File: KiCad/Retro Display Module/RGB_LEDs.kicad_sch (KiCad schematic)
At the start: 25 parts, among them J21 Conn_01x02_Pin, J23 Conn_01x02_Pin, J24 Conn_01x04_Pin, J25 Conn_02x03_Odd_Even, U4 2N7002

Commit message: Updated USB PD and Driver LED circuit
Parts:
- TP1, TP2, TP3: footprint TestPoint:TestPoint_Pad_2.0x2.0mm -> Library:TestPoint_THTPad_2.0x2.0mm_Drill1.0mm
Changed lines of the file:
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@@
       (effects (font (size 1.27 1.27)) (justify left))
     )
-    (property "Footprint" "TestPoint:TestPoint_Pad_2.0x2.0mm" (at 156.21 163.83 0)
+    (property "Footprint" "Library:TestPoint_THTPad_2.0x2.0mm_Drill1.0mm" (at 156.21 163.83 0)
       (effects (font (size 1.27 1.27)) hide)
     )
@@
         )
         (path "/046eef48-6d3f-4288-a12a-fc20b7e12e30/5f242e7d-44cc-4d59-bac4-986620e81512"
-          (reference "#PWR016") (unit 1)
+          (reference "#PWR017") (unit 1)
         )
       )
@@
         )
         (path "/046eef48-6d3f-4288-a12a-fc20b7e12e30/5f242e7d-44cc-4d59-bac4-986620e81512"
-          (reference "#PWR017") (unit 1)
+          (reference "#PWR018") (unit 1)
         )
       )
@@
       (effects (font (size 1.27 1.27)) (justify left))
     )
-    (property "Footprint" "TestPoint:TestPoint_Pad_2.0x2.0mm" (at 87.63 162.56 0)
+    (property "Footprint" "Library:TestPoint_THTPad_2.0x2.0mm_Drill1.0mm" (at 87.63 162.56 0)
       (effects (font (size 1.27 1.27)) hide)
     )
@@
       (effects (font (size 1.27 1.27)) (justify left))
     )
-    (property "Footprint" "TestPoint:TestPoint_Pad_2.0x2.0mm" (at 123.19 162.56 0)
-      (effects (font (size 1.27 1.27)) hide)
-    )
+    (property "Footprint" "Library:TestPoint_THTPad_2.0x2.0mm_Drill1.0mm" (at 123.19 162.56 0)
+      (effects (font (size 1.27 1.27)) hide)
+    )

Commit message: Begin STM32 Programming
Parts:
- removed D1, D11, D13, D15, D17, D19, D21, D3, D5, D7, D9: WS2812B, Library:LED-SMD_4P-L5.0-W5.0-BL_XL-5050RGBC, symbol LED:WS2812B
- added D10, D11, D12, D13, D14, D15, D16, D17, D18, D19, D20, D21, D22, D23, D3, D4, D5, D6, D7, D8, D9: XL-1615RGBC-WS2812B, Library:LED-SMD_4P-L1.6-W1.5_XL-1615RGBC-WS2812B, symbol EEE4022S:XL-1615RGBC-WS2812B
- J21, J23, J24: now left out of the parts list
- TP1, TP2, TP3: now not fitted; now left out of the parts list
- renumbered J25 to J27
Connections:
- net Cheese: now also D5.4 (DI)
- net DIN: now also D3.4 (DI), D4.4 (DI)
- net GND: now also D10.3 (GND), D11.3 (GND), D12.3 (GND), D13.3 (GND), D14.3 (GND), D15.3 (GND), D16.3 (GND), D17.3 (GND), D18.3 (GND), D19.3 (GND), D20.3 (GND), D21.3 (GND), D22.3 (GND), D23.3 (GND), D3.3 (GND), D4.3 (GND), D5.3 (GND), D6.3 (GND), D7.3 (GND), D8.3 (GND), D9.3 (GND)
- net at J21.1 (Pin_1): now also D10.2 (VDD), D11.2 (VDD), D12.2 (VDD), D13.2 (VDD), D14.2 (VDD), D15.2 (VDD), D16.2 (VDD), D17.2 (VDD), D18.2 (VDD), D19.2 (VDD), D20.2 (VDD), D21.2 (VDD), D22.2 (VDD), D23.2 (VDD), D3.2 (VDD), D4.2 (VDD), D6.2 (VDD), D7.2 (VDD), D8.2 (VDD), D9.2 (VDD)
- net at J23.1 (Pin_1), TP3.1: now also D5.1 (DO)
- net at D22.1 (K): now also D5.2 (VDD)
- new net: D12.1 (DO), D14.4 (DI)
- new net: D10.1 (DO), D12.4 (DI)
- new net: D13.1 (DO), D15.4 (DI)
- new net: D11.1 (DO), D13.4 (DI)
- new net: D16.1 (DO), D18.4 (DI)
- new net: D14.1 (DO), D16.4 (DI)
- new net: D19.1 (DO), D21.4 (DI)
- new net: D17.1 (DO), D19.4 (DI)
- new net: D7.1 (DO), D9.4 (DI)
- new net: D4.1 (DO), D7.4 (DI)
- new net: D6.1 (DO), D8.4 (DI)
- new net: D3.1 (DO), D6.4 (DI)
- new net: D15.1 (DO), D17.4 (DI)
- new net: D10.4 (DI), D8.1 (DO)
- new net: D20.1 (DO), D22.4 (DI)
- new net: D18.1 (DO), D20.4 (DI)
- new net: D11.4 (DI), D9.1 (DO)
- new net: D21.1 (DO), D23.4 (DI)
- no-connect marks 1 -> 2
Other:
- moved on the sheet: D22, J21, J23, J24, J27, R5, U4

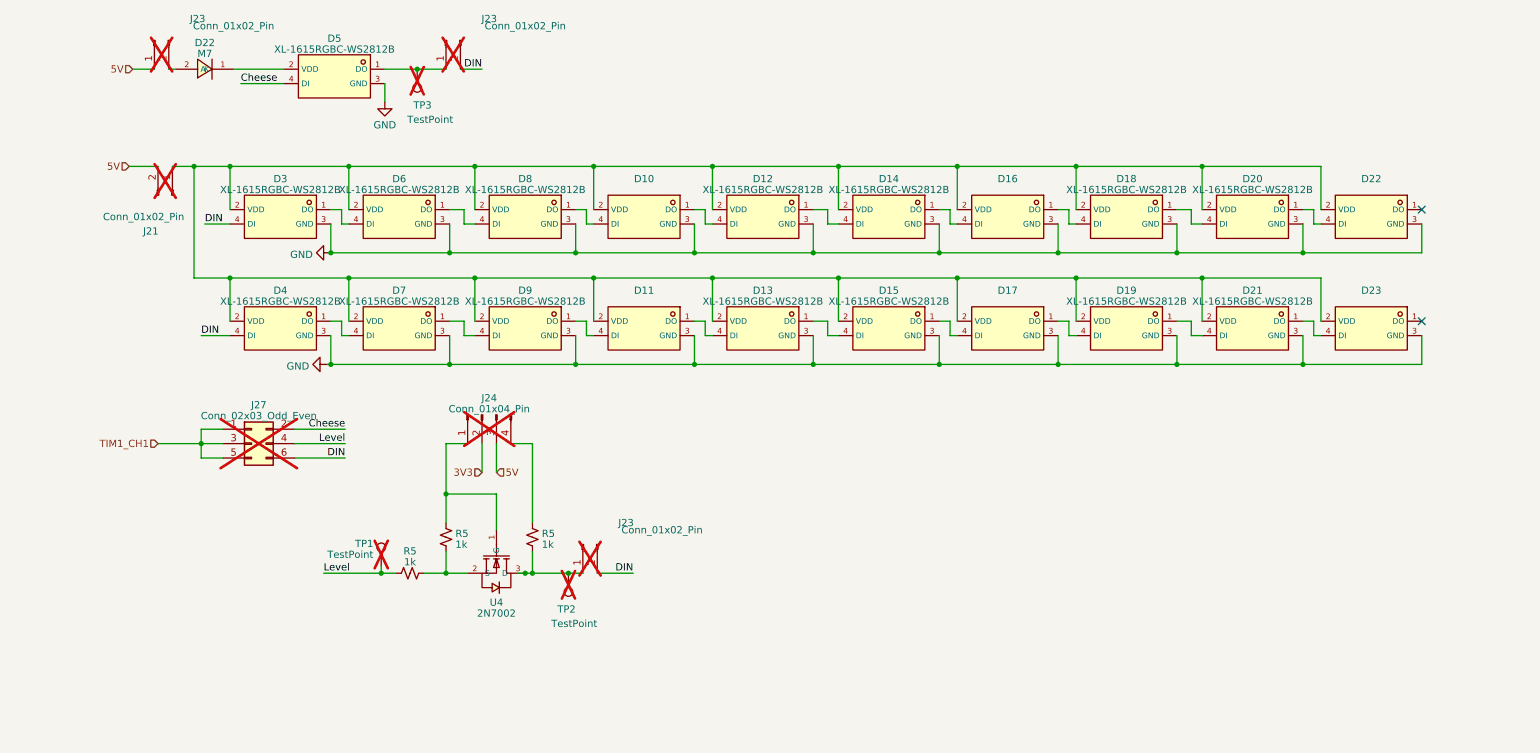
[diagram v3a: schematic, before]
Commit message: Updated Schematics and Added Reverse polarity protection
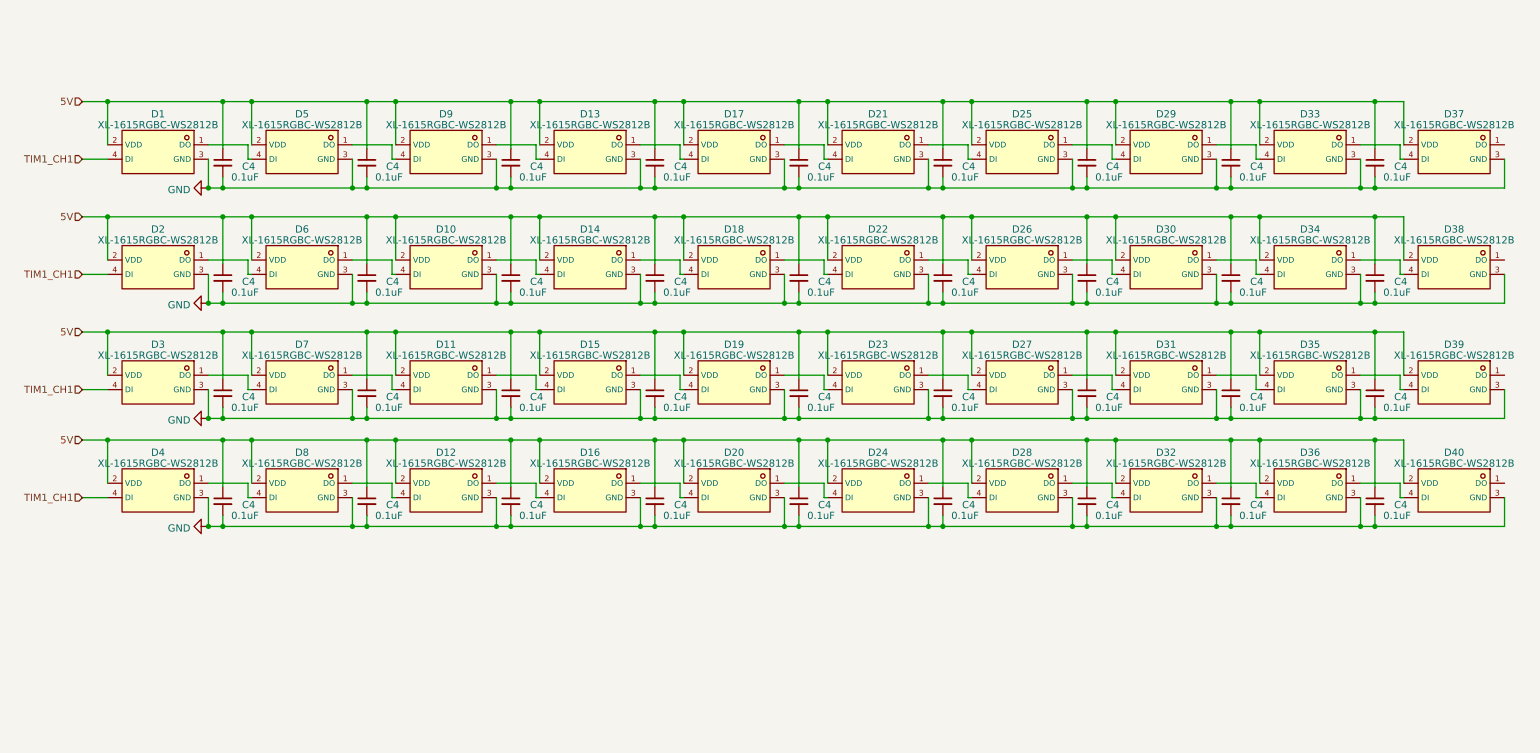
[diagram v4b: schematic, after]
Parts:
- removed D22: M7, Library:SMA_L4.3-W2.6-LS5.2-RD, symbol EEE4022S:M7_C95872
- removed J21, J23 (x3): Conn_01x02_Pin, Connector_PinHeader_2.54mm:PinHeader_1x02_P2.54mm_Vertical, symbol Connector:Conn_01x02_Pin
- removed J24: Conn_01x04_Pin, Connector_PinHeader_2.54mm:PinHeader_1x04_P2.54mm_Vertical, symbol Connector:Conn_01x04_Pin
- removed J27: Conn_02x03_Odd_Even, Connector_PinHeader_2.54mm:PinHeader_2x03_P2.54mm_Vertical, symbol Connector_Generic:Conn_02x03_Odd_Even
- removed R5 (x3): 1k, Resistor_SMD:R_0805_2012Metric, symbol Device:R_Small_US
- removed TP1, TP2, TP3: TestPoint, Library:TestPoint_THTPad_2.0x2.0mm_Drill1.0mm, symbol Connector:TestPoint
- removed U4: 2N7002, Library:SOT-23-3_L2.9-W1.3-P1.90-LS2.4-BR, symbol EEE4022S:AO3400A
- added C4 (x36): 0.1uF, Library:C_0402_1005Metric_Pad0.74x0.62mm_HandSolder, symbol Device:C_Small
- added D2, D24, D25, D26, D27, D28, D29, D3, D30, D31, D32, D33, D34, D35, D36, D37, D38, D39, D40: XL-1615RGBC-WS2812B, Library:LED-SMD_4P-L1.6-W1.5_XL-1615RGBC-WS2812B, symbol EEE4022S:XL-1615RGBC-WS2812B
- renumbered D3 to D1
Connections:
- net Cheese is gone; now on an unnamed net: D5.4 (DI)
- net DIN is gone; now on net TIM1_CH1: D1.4 (DI), D4.4 (DI)
- net 5V: now also D1.2 (VDD), D10.2 (VDD), D11.2 (VDD), D12.2 (VDD), D13.2 (VDD), D14.2 (VDD), D15.2 (VDD), D16.2 (VDD), D17.2 (VDD), D18.2 (VDD), D19.2 (VDD), D20.2 (VDD), D21.2 (VDD), D22.2 (VDD), D23.2 (VDD), D4.2 (VDD), D5.2 (VDD), D6.2 (VDD), D7.2 (VDD), D8.2 (VDD), D9.2 (VDD), C4.1, C4.1, C4.1, C4.1, C4.1, C4.1, C4.1, C4.1, C4.1, C4.1, C4.1, C4.1, C4.1, C4.1, C4.1, C4.1, C4.1, C4.1, C4.1, C4.1, C4.1, C4.1, C4.1, C4.1, C4.1, C4.1, C4.1, C4.1, C4.1, C4.1, C4.1, C4.1, C4.1, C4.1, C4.1, C4.1, D2.2 (VDD), D24.2 (VDD), D25.2 (VDD), D26.2 (VDD), D27.2 (VDD), D28.2 (VDD), D29.2 (VDD), D3.2 (VDD), D30.2 (VDD), D31.2 (VDD), D32.2 (VDD), D33.2 (VDD), D34.2 (VDD), D35.2 (VDD), D36.2 (VDD), D37.2 (VDD), D38.2 (VDD), D39.2 (VDD), D40.2 (VDD)
- net GND: now also C4.2, C4.2, C4.2, C4.2, C4.2, C4.2, C4.2, C4.2, C4.2, C4.2, C4.2, C4.2, C4.2, C4.2, C4.2, C4.2, C4.2, C4.2, C4.2, C4.2, C4.2, C4.2, C4.2, C4.2, C4.2, C4.2, C4.2, C4.2, C4.2, C4.2, C4.2, C4.2, C4.2, C4.2, C4.2, C4.2, D2.3 (GND), D24.3 (GND), D25.3 (GND), D26.3 (GND), D27.3 (GND), D28.3 (GND), D29.3 (GND), D3.3 (GND), D30.3 (GND), D31.3 (GND), D32.3 (GND), D33.3 (GND), D34.3 (GND), D35.3 (GND), D36.3 (GND), D37.3 (GND), D38.3 (GND), D39.3 (GND), D40.3 (GND)
- net TIM1_CH1: now also D2.4 (DI), D3.4 (DI)
- net at D5.1 (DO): now also D9.4 (DI)
- net at D14.4 (DI): now also D10.1 (DO); no longer D12.1 (DO)
- net at D12.4 (DI): now also D8.1 (DO); no longer D10.1 (DO)
- net at D15.4 (DI): now also D11.1 (DO); no longer D13.1 (DO)
- net at D13.4 (DI): now also D9.1 (DO); no longer D11.1 (DO)
- net at D18.4 (DI): now also D14.1 (DO); no longer D16.1 (DO)
- net at D16.4 (DI): now also D12.1 (DO); no longer D14.1 (DO)
- net at D21.4 (DI): now also D17.1 (DO); no longer D19.1 (DO)
- net at D19.4 (DI): now also D15.1 (DO); no longer D17.1 (DO)
- net at D7.1 (DO): now also D11.4 (DI); no longer D9.4 (DI)
- net at D4.1 (DO): now also D8.4 (DI); no longer D7.4 (DI)
- net at D6.1 (DO): now also D10.4 (DI); no longer D8.4 (DI)
- net at D1.1 (DO): no longer D6.4 (DI)
- net at D17.4 (DI): now also D13.1 (DO); no longer D15.1 (DO)
- net at D22.4 (DI): now also D18.1 (DO); no longer D20.1 (DO)
- net at D20.4 (DI): now also D16.1 (DO); no longer D18.1 (DO)
- net at D22.1 (DO): now also D26.4 (DI)
- net at D21.1 (DO): now also D25.4 (DI); no longer D23.4 (DI)
- net at D23.1 (DO): now also D27.4 (DI)
- new net: D30.1 (DO), D34.4 (DI)
- new net: D26.1 (DO), D30.4 (DI)
- new net: D35.1 (DO), D39.4 (DI)
- new net: D2.1 (DO), D6.4 (DI)
- new net: D20.1 (DO), D24.4 (DI)
- new net: D36.1 (DO), D40.4 (DI)
- new net: D32.1 (DO), D36.4 (DI)
- new net: D29.1 (DO), D33.4 (DI)
- new net: D25.1 (DO), D29.4 (DI)
- new net: D31.1 (DO), D35.4 (DI)
- new net: D34.1 (DO), D38.4 (DI)
- new net: D33.1 (DO), D37.4 (DI)
- new net: D3.1 (DO), D7.4 (DI)
- new net: D19.1 (DO), D23.4 (DI)
- new net: D28.1 (DO), D32.4 (DI)
- new net: D24.1 (DO), D28.4 (DI)
- new net: D27.1 (DO), D31.4 (DI)
- no-connect marks 2 -> 0
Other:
- moved on the sheet: D1
